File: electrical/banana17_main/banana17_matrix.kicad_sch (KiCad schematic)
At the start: 38 parts, among them SW1 SW, SW10 SW, SW11 SW, SW12 SW, SW13 SW, SW14 SW, SW15 SW, SW16 SW, SW17 SW, SW2 SW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

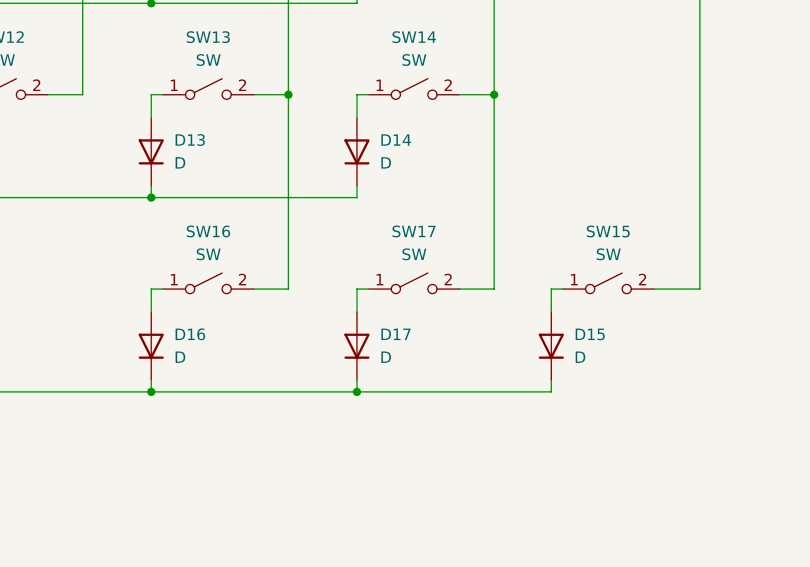
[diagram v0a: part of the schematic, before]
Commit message: Preliminary matrix complete. Need to do encoders next.
Preliminary matrix complete. Need to do encoders next.
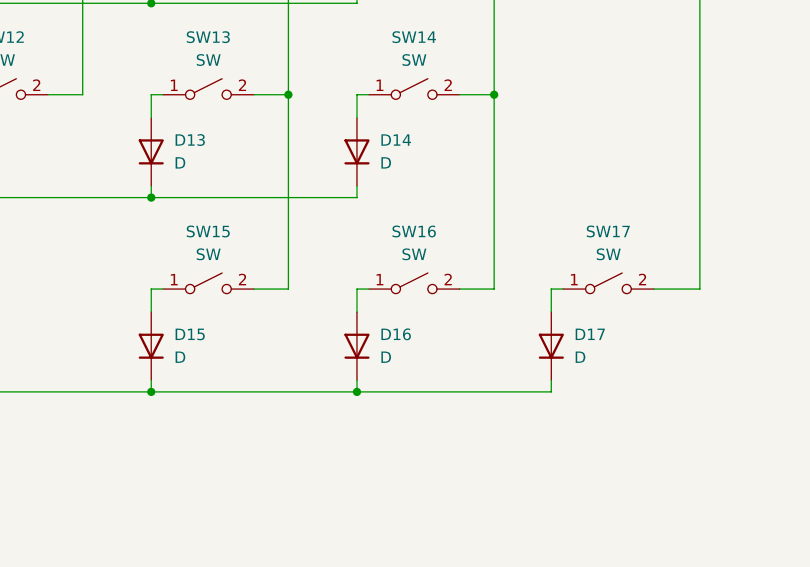
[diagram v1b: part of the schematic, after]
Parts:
- renumbered D16 to D15, D17 to D16, D15 to D17, SW16 to SW15, SW17 to SW16, SW15 to SW17
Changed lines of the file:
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@@
 		(dnp no)
 		(fields_autoplaced yes)
-		(property "Reference" "SW15"
+		(property "Reference" "SW17"
 			(at 165.1 151.13 0)
 			(effects
@@
 			(project "banana17_main"
 				(path "/fd2b462c-d7c2-4bbf-9a41-8b3fef737a65/8f16a207-73c4-47aa-9ecc-1f36a96752ff"
-					(reference "SW15")
+					(reference "SW17")
 					(unit 1)
 				)
@@
 		(dnp no)
 		(fields_autoplaced yes)
-		(property "Reference" "SW16"
+		(property "Reference" "SW15"
 			(at 120.65 151.13 0)
 			(effects
@@
 			(project "banana17_main"
 				(path "/fd2b462c-d7c2-4bbf-9a41-8b3fef737a65/8f16a207-73c4-47aa-9ecc-1f36a96752ff"
-					(reference "SW16")
+					(reference "SW15")
 					(unit 1)
 				)
@@
 		(dnp no)
 		(fields_autoplaced yes)
-		(property "Reference" "SW17"
+		(property "Reference" "SW16"
 			(at 143.51 151.13 0)
 			(effects
@@
 			(project "banana17_main"
 				(path "/fd2b462c-d7c2-4bbf-9a41-8b3fef737a65/8f16a207-73c4-47aa-9ecc-1f36a96752ff"
-					(reference "SW17")
+					(reference "SW16")
 					(unit 1)
 				)
@@
 		(dnp no)
 		(fields_autoplaced yes)
-		(property "Reference" "#PWR022"
+		(property "Reference" "#PWR024"
 			(at 86.36 114.3 0)
 			(effects
@@
 			(project "banana17_main"
 				(path "/fd2b462c-d7c2-4bbf-9a41-8b3fef737a65/8f16a207-73c4-47aa-9ecc-1f36a96752ff"
-					(reference "#PWR022")
+					(reference "#PWR024")
 					(unit 1)
 				)
@@
 		(dnp no)
 		(fields_autoplaced yes)
-		(property "Reference" "D15"
+		(property "Reference" "D17"
 			(at 161.29 162.5599 90)
 			(effects
@@
 			(project "banana17_main"
 				(path "/fd2b462c-d7c2-4bbf-9a41-8b3fef737a65/8f16a207-73c4-47aa-9ecc-1f36a96752ff"
-					(reference "D15")
+					(reference "D17")
 					(unit 1)
 				)
@@
 		(dnp no)
 		(fields_autoplaced yes)
-		(property "Reference" "D17"
+		(property "Reference" "D16"
 			(at 139.7 162.5599 90)
 			(effects
@@
 			(project "banana17_main"
 				(path "/fd2b462c-d7c2-4bbf-9a41-8b3fef737a65/8f16a207-73c4-47aa-9ecc-1f36a96752ff"
-					(reference "D17")
+					(reference "D16")
 					(unit 1)
 				)
@@
 		(dnp no)
 		(fields_autoplaced yes)
-		(property "Reference" "D16"
+		(property "Reference" "D15"
 			(at 116.84 162.5599 90)
 			(effects
@@
 			(project "banana17_main"
 				(path "/fd2b462c-d7c2-4bbf-9a41-8b3fef737a65/8f16a207-73c4-47aa-9ecc-1f36a96752ff"
-					(reference "D16")
+					(reference "D15")
 					(unit 1)
 				)
@@
 		(dnp no)
 		(fields_autoplaced yes)
-		(property "Reference" "#PWR023"
+		(property "Reference" "#PWR025"
 			(at 86.36 135.89 0)
 			(effects
@@
 			(project "banana17_main"
 				(path "/fd2b462c-d7c2-4bbf-9a41-8b3fef737a65/8f16a207-73c4-47aa-9ecc-1f36a96752ff"
-					(reference "#PWR023")
-					(unit 1)
-				)
+					(reference "#PWR025")
+					(unit 1)
+				)

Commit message: Initial PCB complete.
Initial PCB complete.
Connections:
- net COL5 is gone; now on net COL4: SW17.2 (B), SW4.2 (B), SW8.2 (B)
- net COL0: no longer ENC2.S2
- net COL4: no longer SW11.2 (B), SW14.2 (B), SW16.2 (B), SW3.2 (B), SW7.2 (B)
- net ROW2: no longer ENC_D1.1 (K)
- net ROW3: no longer ENC_D2.1 (K)
- new net COL3: SW11.2 (B), SW14.2 (B), SW16.2 (B), SW3.2 (B), SW7.2 (B)
- new net ROW5: ENC2.S2, ENC_D1.1 (K)
- new net ROW6: ENC_D2.1 (K)
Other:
- moved on the sheet: D1, D10, D11, D12, D13, D14, D15, D16, D17, D2, D3, D4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

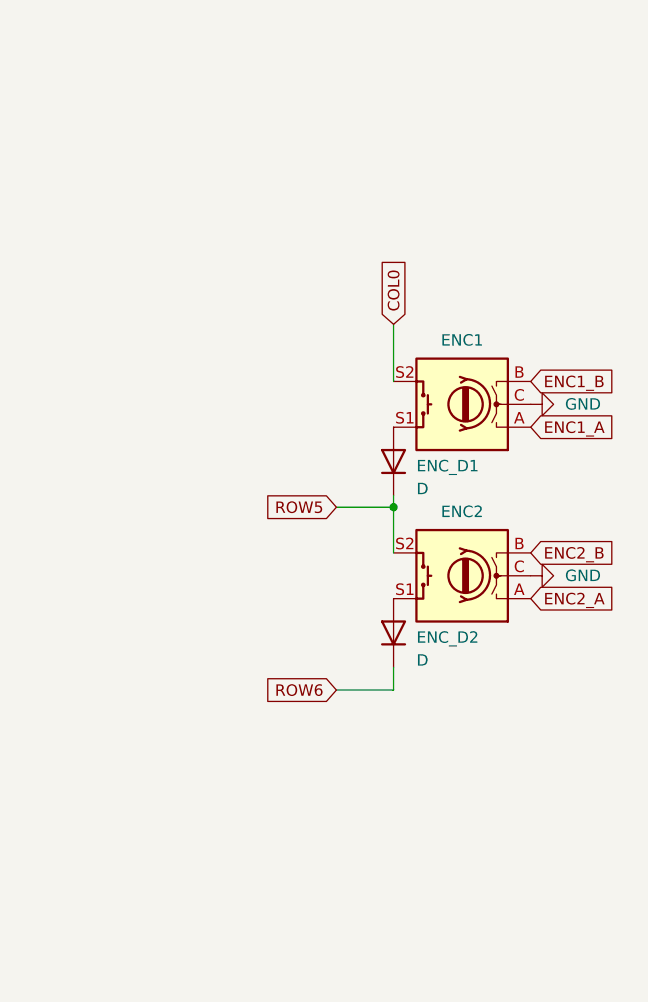
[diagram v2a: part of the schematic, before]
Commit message: Reduce PCB size less than 100mm x 100m for cheaper PCB.
Reduce PCB size less than 100mm x 100m for cheaper PCB.
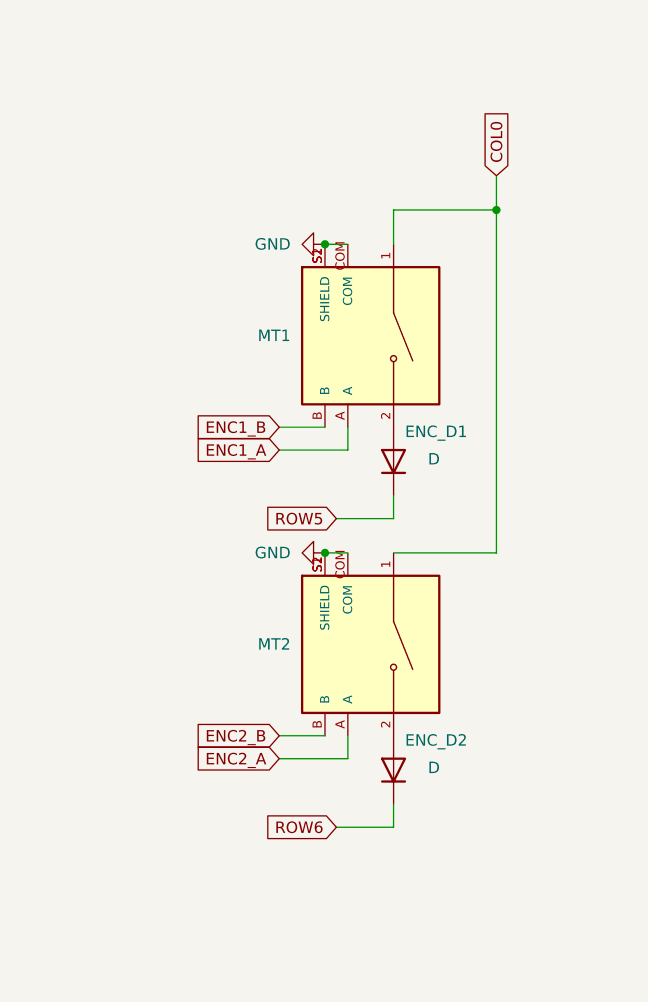
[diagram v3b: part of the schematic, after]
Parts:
- removed ENC1, ENC2: RotaryEncoder_Switch, Rotary_Encoder:RotaryEncoder_Alps_EC11E-Switch_Vertical_H20mm, symbol Device:RotaryEncoder_Switch
- added MT1, MT2: PEC11R-4215F-S0024, PEC11R-4215K:XDCR_PEC11R-4215F-S0024, symbol PEC11R-4215F-S0024:PEC11R-4215F-S0024
- SW15: footprint MX_Hotswap:MX-Hotswap-2U -> MX_Hotswap:MX-Hotswap-2U-ReversedStabilizers
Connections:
- net COL0: now also MT1.1, MT2.1
- net ENC1_A: now also MT1.A
- net ENC1_B: now also MT1.B
- net ENC2_A: now also MT2.A
- net ENC2_B: now also MT2.B
- net GND: now also MT1.COM, MT1.S1 (SHIELD), MT1.S2 (SHIELD), MT2.COM, MT2.S1 (SHIELD), MT2.S2 (SHIELD)
- net at ENC_D2.2 (A): now also MT2.2
- net at ENC_D1.2 (A): now also MT1.2
